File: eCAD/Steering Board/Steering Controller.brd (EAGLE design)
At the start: 45.4 x 58.4 mm, 22 parts, among them Y1 12MHz

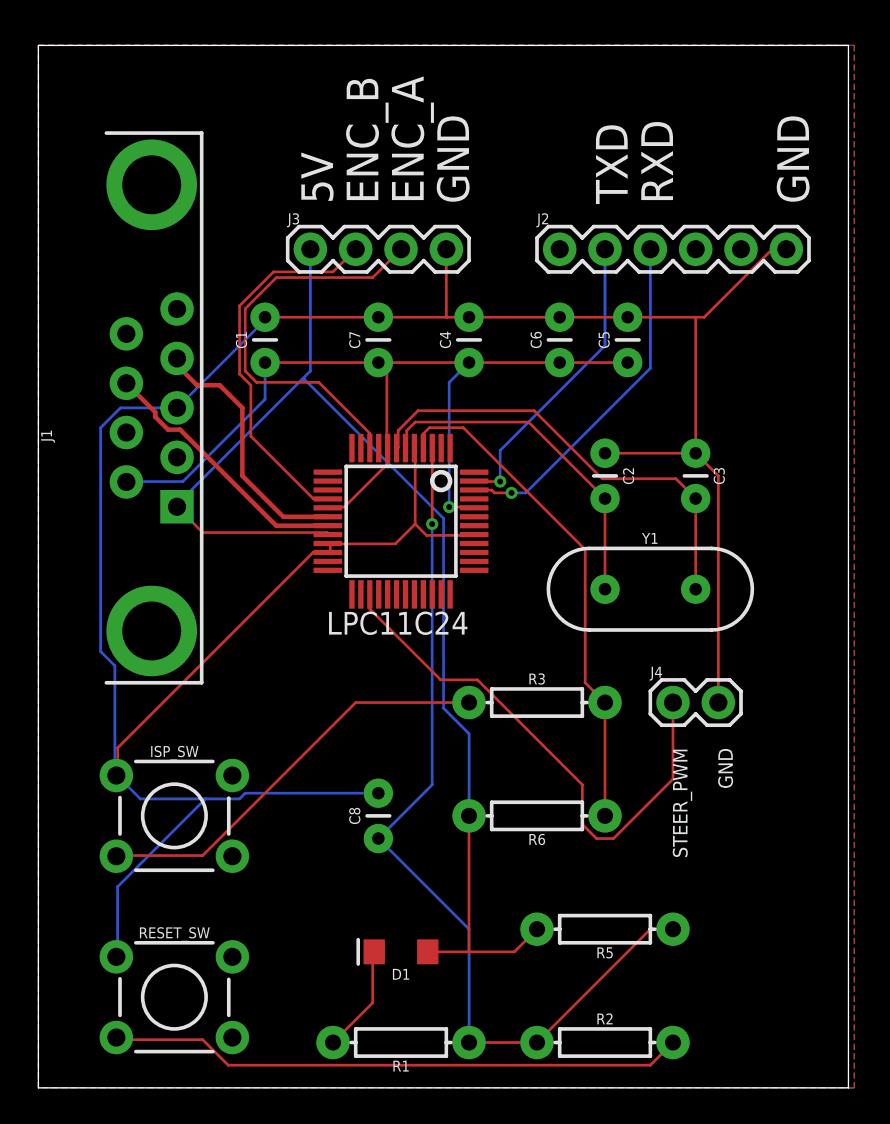
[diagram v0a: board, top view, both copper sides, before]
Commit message: Added new pin headers & tri-state buffers
-New 3-pin header to communicate with NAND Servo
-Removed Obsolete 2pin header
-Updated DB9 and UART
-Added Tri-State Buffers to control TXD/RXD data flow.
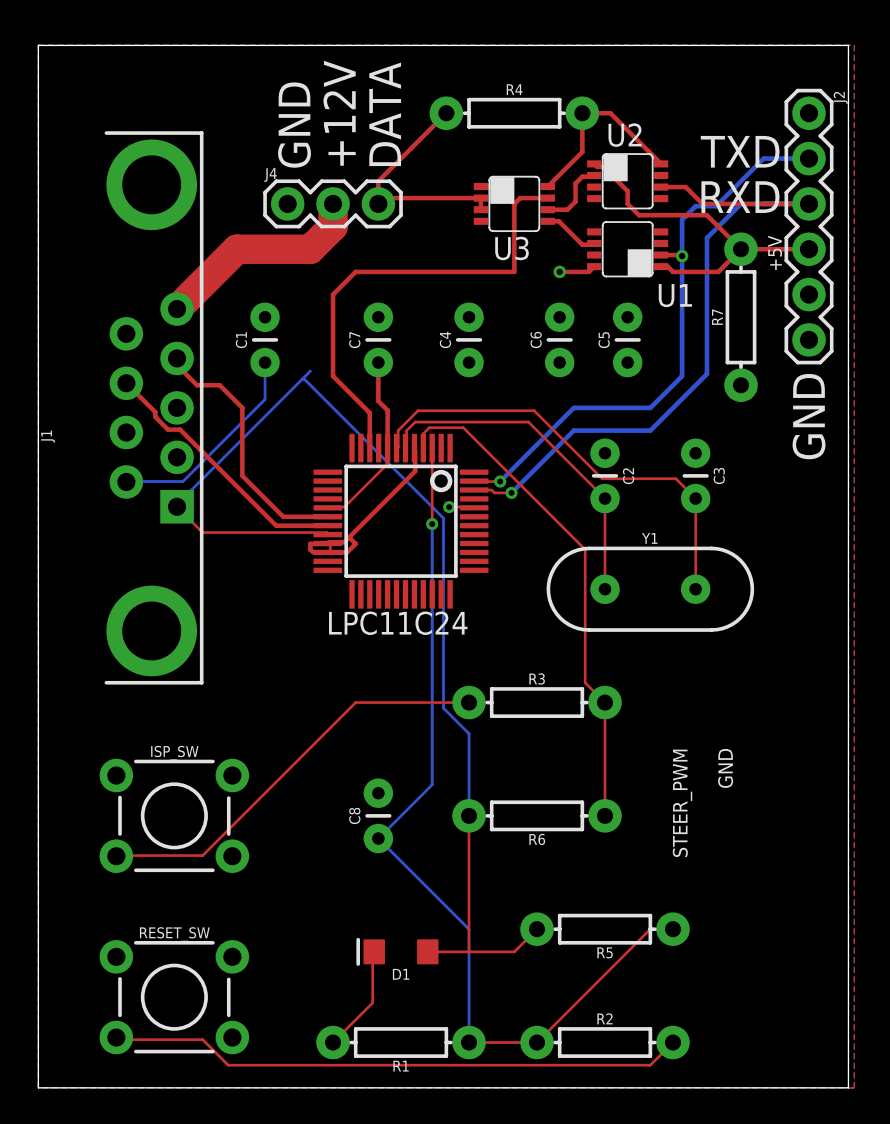
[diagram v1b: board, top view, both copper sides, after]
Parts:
- removed J3: (no value), SparkFun-Connectors:1X04
- added R4, R7: 10k, SparkFun-Resistors:AXIAL-0.3
- added U1, U2, U3: SN74LVC2G241, AdamLibrary:TI_S8
- J4: device SparkFun-Connectors:1X02 -> SparkFun-Connectors:1X03
- moved J4 35.3 mm to (14.0, 53.3)
- moved J2 15.9 mm to (43.2, 58.4), turned to 270 degrees
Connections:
- removed net ENC_A: J3.3, LPC11C24.10
- removed net ENC_B: J3.2, LPC11C24.16
- removed net STEER_PWM: J4.1, LPC11C24.27
- new net +12V: J1.5, J4.2
- new net DATA: J4.3, R4.P$1, U3.2, U3.3
- new net N$3: U2.2, U3.6
- new net N$5: U1.6, U3.5
- new net TX_ENABLE: LPC11C24.10, U3.1, U3.7
- new net UART_5V: J2.4, R7.P$2, U1.1, U2.1
- net 3.3V: now also R4.P$2, U1.8, U2.8, U3.8
- net CAN_5V: no longer J3.1
- net GND: now also J4.1, R7.P$1, U1.3, U1.4, U1.5, U1.7, U2.3, U2.4, U2.5, U2.7, U3.4; no longer J3.4, J4.2
- net RXD: now also U2.6
- net TXD: now also U1.2
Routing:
- net GND: track 151.5 -> 13.8 mm
- net STEER_PWM: track 30.1 -> 0.00 mm
- net TX_ENABLE: track 0.00 -> 28.2 mm
- net ENC_A: track 22.9 -> 0.00 mm
- net RXD: track 19.5 -> 41.2 mm
- net ENC_B: track 21.2 -> 0.00 mm
- net UART_5V: track 0.00 -> 19.6 mm
- net 3.3V: track 52.3 -> 36.0 mm, vias 1 -> 2
- net TXD: track 16.9 -> 32.6 mm, vias 1 -> 2
- net DATA: track 0.00 -> 13.2 mm
- net +12V: track 0.00 -> 11.9 mm
- net CAN_5V: track 69.3 -> 62.5 mm
- net N$3: track 0.00 -> 3.99 mm
- net N$5: track 0.00 -> 3.17 mm
- added copper zone on layer 16, net 3.3V
- removed copper zone on layer 16, net GND
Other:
- board text added: "+12V"
- board text added: "+5V"
- board text added: "DATA"
- board text removed: "5V"
- board text removed: "ENC_A"
- board text removed: "ENC_B"
